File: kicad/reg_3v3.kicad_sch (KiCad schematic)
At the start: 3 parts

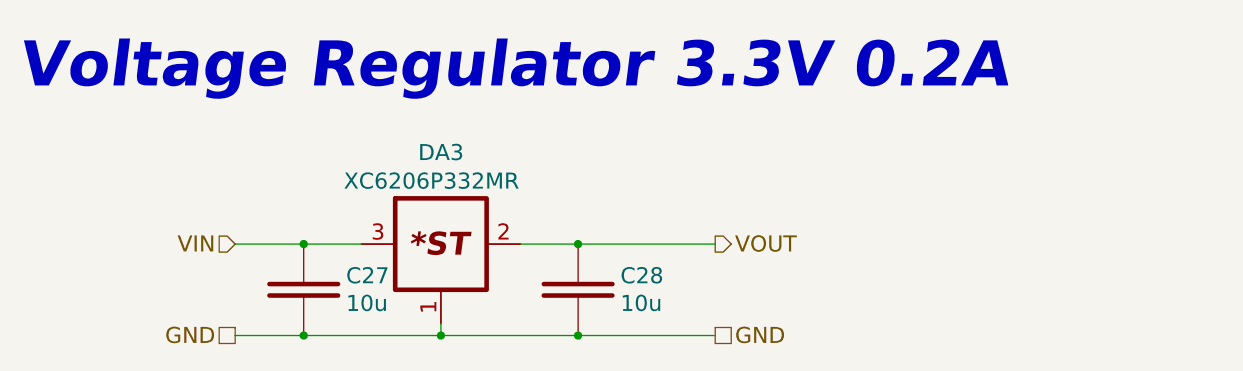
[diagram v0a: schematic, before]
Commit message: Reannotate schematic; Fix 5032 crystal footprint field; Update PCB with 5032 crystal
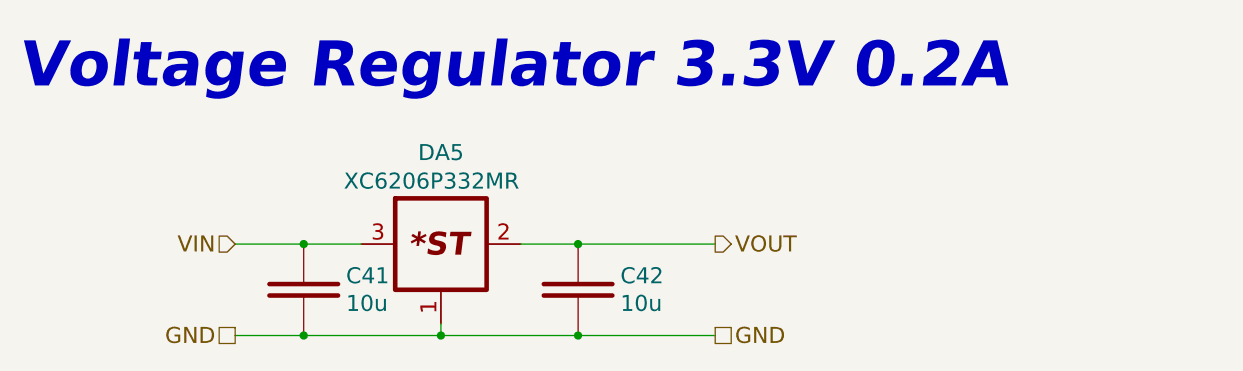
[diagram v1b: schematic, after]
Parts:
- renumbered C27 to C41, C28 to C42, DA3 to DA5
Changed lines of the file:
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@@
   (symbol (lib_id "Capacitors:C_CAP") (at 163.068 97.79 270) (unit 1)
     (in_bom yes) (on_board yes)
-    (property "Reference" "C28" (id 0) (at 167.767 96.2406 90)
+    (property "Reference" "C42" (id 0) (at 167.767 96.2406 90)
       (effects (font (size 1.778 1.778)) (justify left))
     )
@@
   (symbol (lib_id "Chips:XC6206P332MR") (at 147.828 92.71 0) (unit 1)
     (in_bom yes) (on_board yes)
-    (property "Reference" "DA3" (id 0) (at 145.288 82.55 0)
+    (property "Reference" "DA5" (id 0) (at 145.288 82.55 0)
       (effects (font (size 1.778 1.778)) (justify left))
     )
@@
   (symbol (lib_id "Capacitors:C_CAP") (at 132.588 97.79 270) (unit 1)
     (in_bom yes) (on_board yes)
-    (property "Reference" "C27" (id 0) (at 137.287 96.2406 90)
+    (property "Reference" "C41" (id 0) (at 137.287 96.2406 90)
       (effects (font (size 1.778 1.778)) (justify left))
     )

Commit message: Add voltage value to caps, update BOM, SCH, ASM
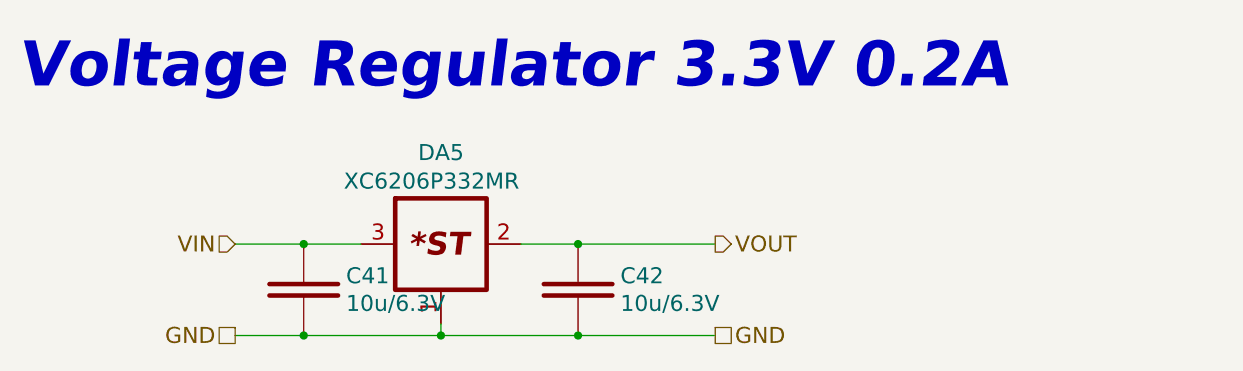
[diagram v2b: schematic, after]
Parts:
- C41, C42: value 10u -> 10u/6.3V; Case/Package (none) -> 0603; Tolerance (none) -> ±10%; Type (none) -> X7R
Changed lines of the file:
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@@
     (effects (font (size 1.778 1.778)) (justify right))
   )
-  (symbol (lib_id "Capacitors:C_CAP") (at 163.068 97.79 270) (unit 1)
+  (symbol (lib_name "C_CAP_1") (lib_id "Capacitors:C_CAP") (at 163.068 97.79 270) (unit 1)
     (in_bom yes) (on_board yes)
     (property "Reference" "C42" (id 0) (at 167.767 96.2406 90)
       (effects (font (size 1.778 1.778)) (justify left))
     )
-    (property "Value" "10u" (id 1) (at 167.767 99.314 90)
+    (property "Value" "10u/6.3V" (id 1) (at 167.767 99.314 90)
       (effects (font (size 1.778 1.778)) (justify left))
     )
@@
     (property "Assembly" "" (id 4) (at 154.178 97.79 0)
       (effects (font (size 1.778 1.778)))
+    )
+    (property "Voltage" "" (id 5) (at 163.068 97.79 0)
+      (effects (font (size 1.27 1.27)) hide)
+    )
+    (property "Case/Package" "0603" (id 6) (at 163.068 97.79 0)
+      (effects (font (size 1.27 1.27)) hide)
+    )
+    (property "Type" "X7R" (id 7) (at 152.908 97.79 0)
+      (effects (font (size 1.27 1.27)) hide)
+    )
+    (property "Tolerance" "±10%" (id 8) (at 150.368 97.79 0)
+      (effects (font (size 1.27 1.27)) hide)
     )
     (pin "1")
@@
       (effects (font (size 1.778 1.778)) (justify left))
     )
-    (property "Value" "10u" (id 1) (at 137.287 99.314 90)
+    (property "Value" "10u/6.3V" (id 1) (at 137.287 99.314 90)
       (effects (font (size 1.778 1.778)) (justify left))
     )
@@
       (effects (font (size 1.778 1.778)))
     )
+    (property "Voltage" "" (id 5) (at 132.588 97.79 0)
+      (effects (font (size 1.27 1.27)) hide)
+    )
+    (property "Case/Package" "0603" (id 6) (at 132.588 97.79 0)
+      (effects (font (size 1.27 1.27)) hide)
+    )
+    (property "Type" "X7R" (id 7) (at 122.428 97.79 0)
+      (effects (font (size 1.27 1.27)) hide)
+    )
+    (property "Tolerance" "±10%" (id 8) (at 119.888 97.79 0)
+      (effects (font (size 1.27 1.27)) hide)
+    )
     (pin "1")

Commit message: Add wiring diagram; Add work ours (stage 2); refactor folders
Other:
- title: (none) -> RadioSens v1
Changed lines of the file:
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@@
 (kicad_sch (version 20211123) (generator eeschema)
   (paper "A4")
+  (title_block
+    (title "RadioSens v1")
+    (comment 2 "Electrical Circuit")
+  )
   (junction (at 163.068 92.71) (diameter 0) (color 0 0 0 0)
   )
